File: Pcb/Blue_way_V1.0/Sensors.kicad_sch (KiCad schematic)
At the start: 0 parts

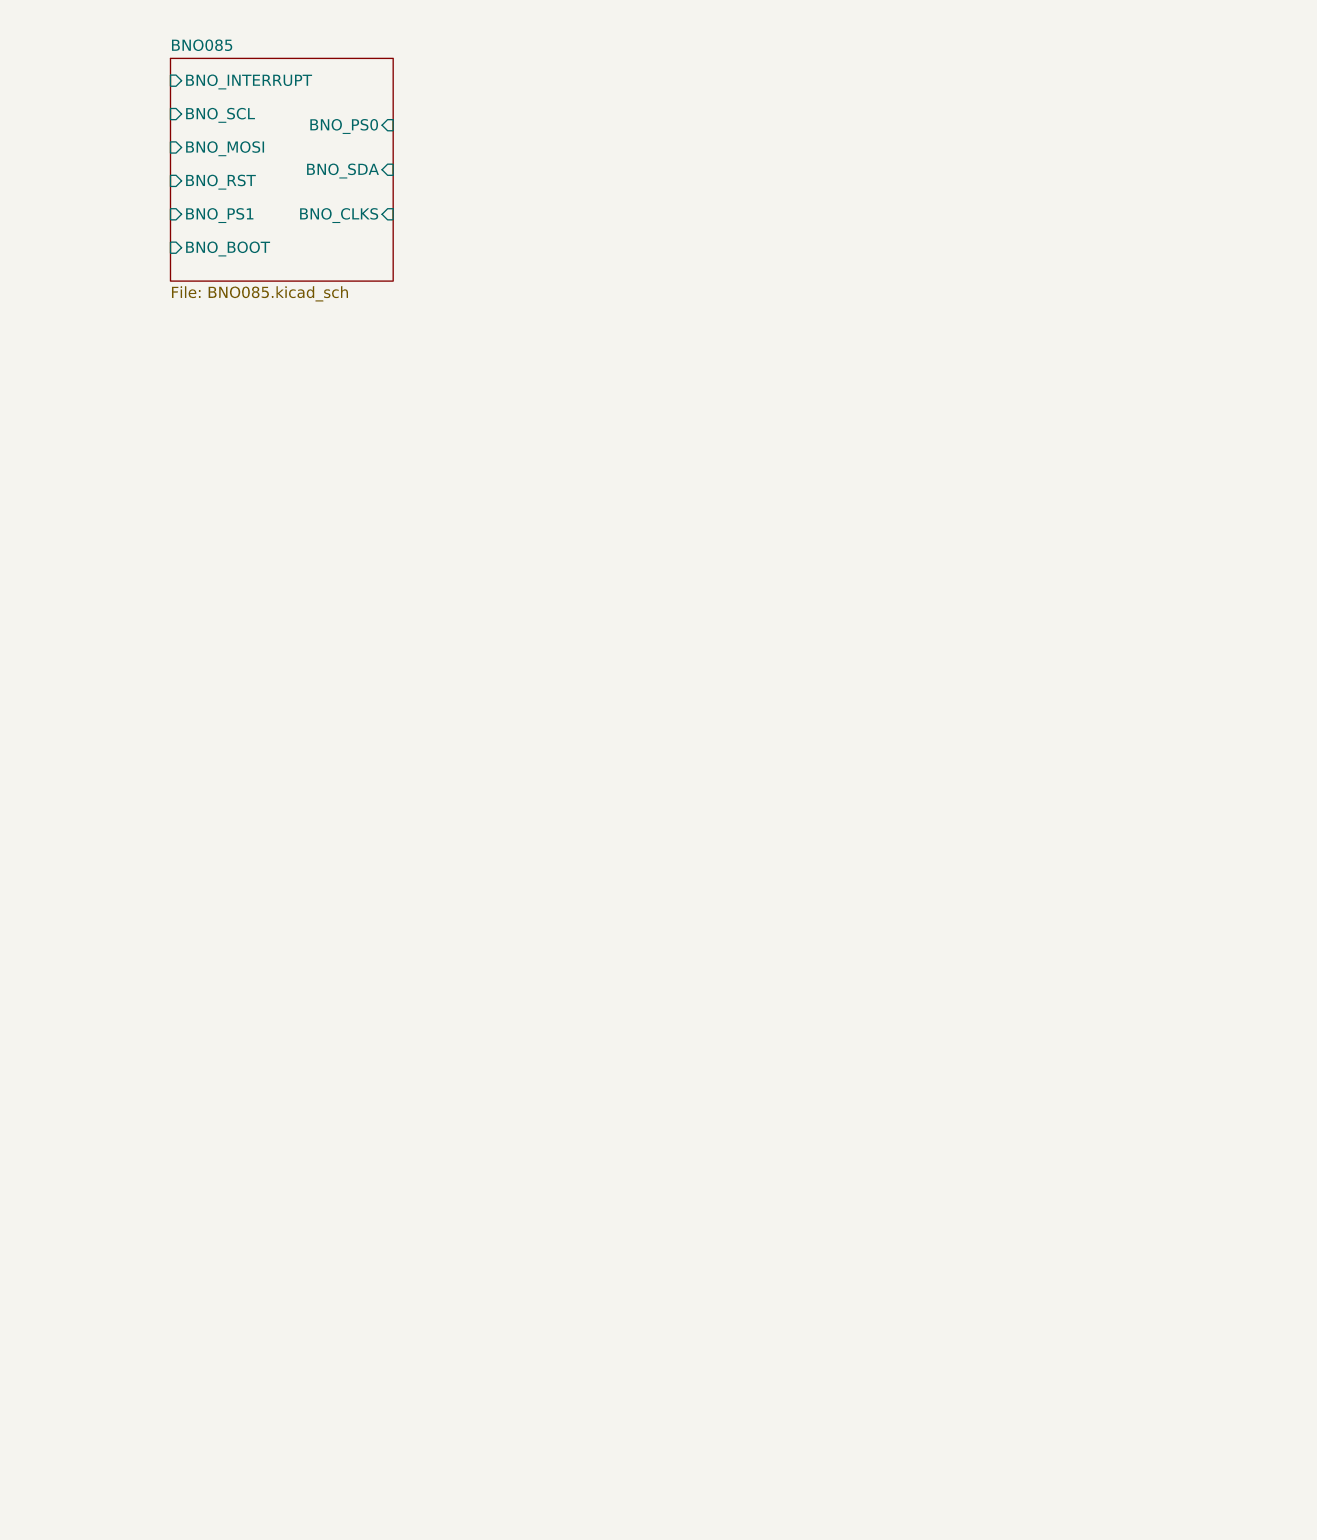
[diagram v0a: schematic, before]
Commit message: SHT and BMP Added with LoRa Comm Module
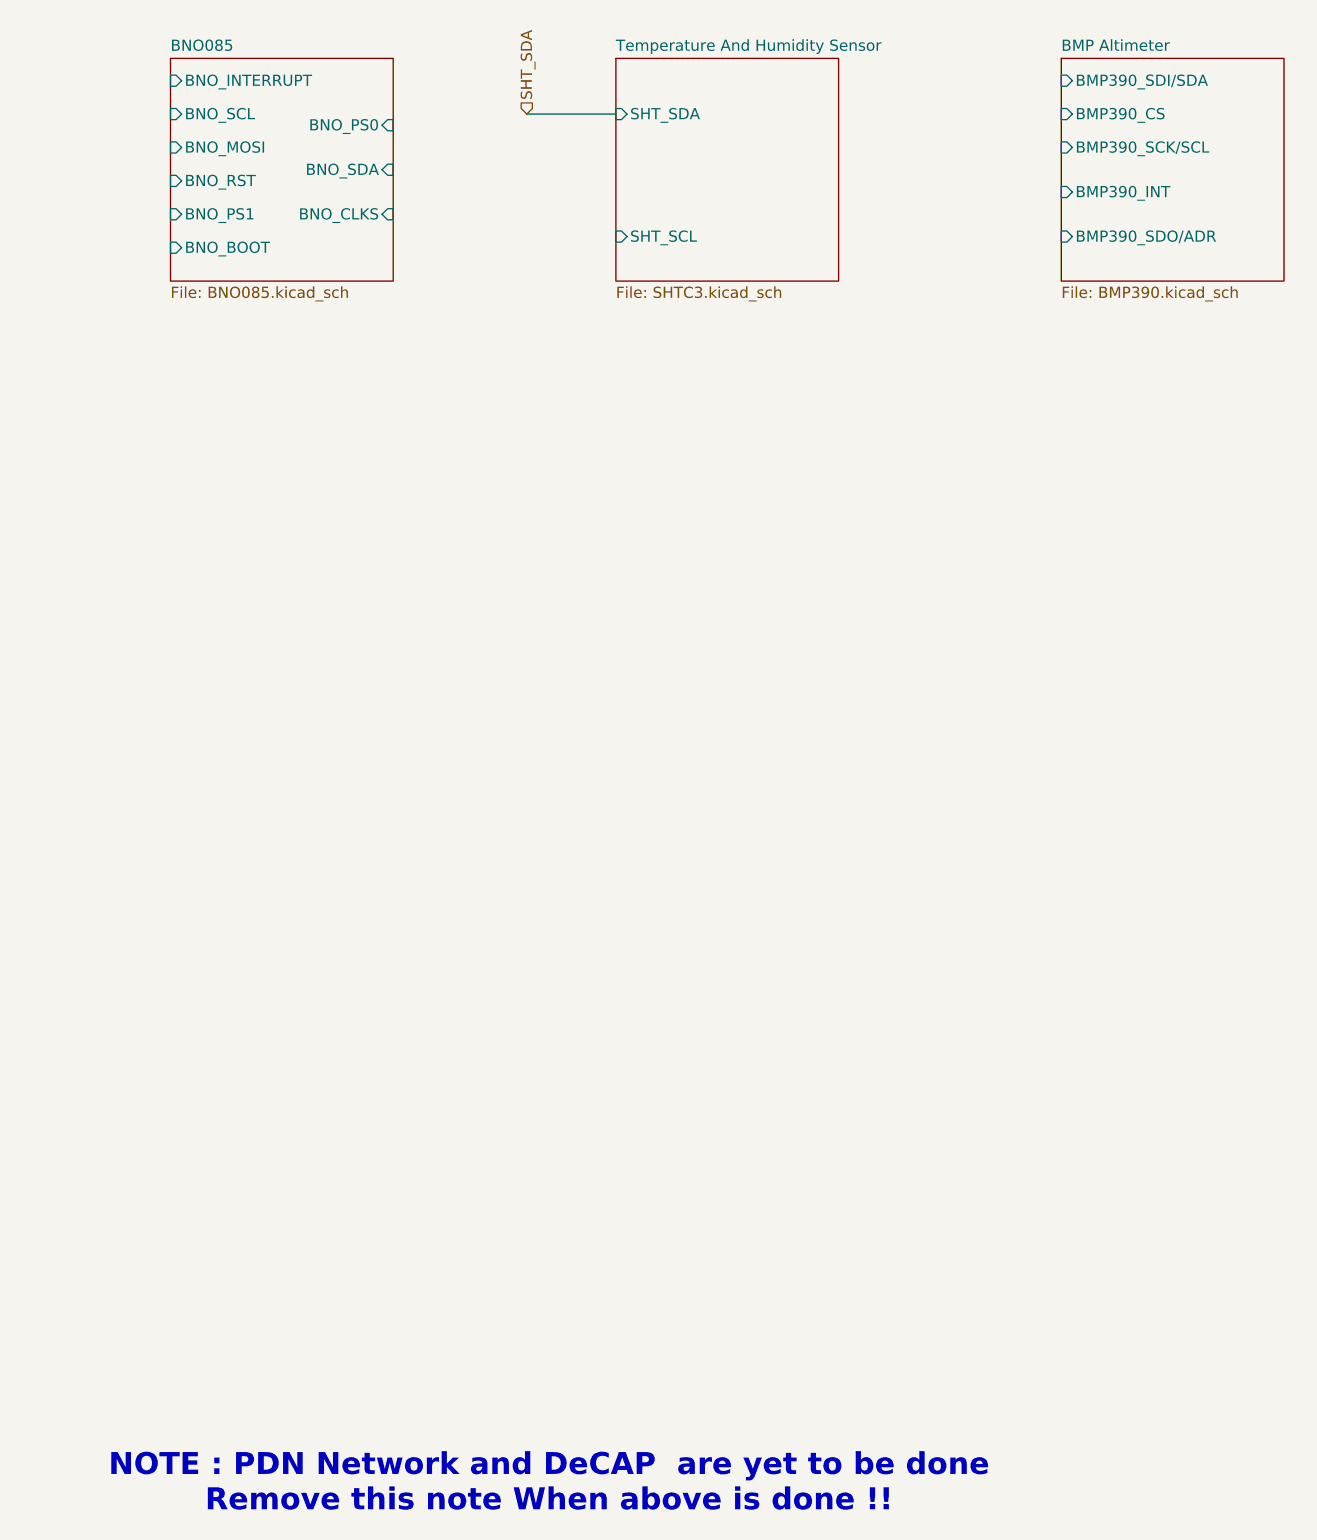
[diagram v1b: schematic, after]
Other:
- added sheet BMP Altimeter (BMP390.kicad_sch)
- added sheet Temperature And Humidity Sensor (SHTC3.kicad_sch)
- note added: "NOTE : PDN Network and DeCAP are yet to be done Remove this note When above is done !!"
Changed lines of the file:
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@@
 		(comment 1 "www.bluewayhorizon.in")
+	)
+	(text "NOTE : PDN Network and DeCAP  are yet to be done\nRemove this note When above is done !!"
+		(exclude_from_sim no)
+		(at 68.58 187.96 0)
+		(effects
+			(font
+				(size 2.5 2.5)
+				(thickness 0.5)
+				(bold yes)
+			)
+		)
+	)
+	(wire
+		(pts
+			(xy 66.04 31.75) (xy 76.2 31.75)
+		)
+		(stroke
+			(width 0)
+			(type default)
+		)
+	)
+	(hierarchical_label "SHT_SDA"
+		(shape input)
+		(at 66.04 31.75 90)
+		(effects
+			(font
+				(size 1.27 1.27)
+			)
+			(justify left)
+		)
 	)
 	(sheet
@@
 				)
 			)
+		)
+	)
+	(sheet
+		(at 127 25.4)
+		(size 25.4 25.4)
+		(exclude_from_sim no)
+		(in_bom yes)
+		(on_board yes)
+		(dnp no)
+		(fields_autoplaced yes)
+		(stroke
+			(width 0.1524)
+			(type solid)
+		)
+		(fill
+			(color 0 0 0 0.0000)
+		)
+		(property "Sheetname" "BMP Altimeter"
+			(at 127 24.6884 0)
+			(effects
+				(font
+					(size 1.27 1.27)
+				)
+				(justify left bottom)
+			)
+		)
+		(property "Sheetfile" "BMP390.kicad_sch"
+			(at 127 51.3846 0)
+			(effects
+				(font
+					(size 1.27 1.27)
+				)
+				(justify left top)
+			)
+		)
+		(pin "BMP390_SDI/SDA" input
+			(at 127 27.94 180)
+			(effects
+				(font
+					(size 1.27 1.27)
+				)
+				(justify left)
+			)
+		)
+		(pin "BMP390_CS" input
+			(at 127 31.75 180)
+			(effects
+				(font
+					(size 1.27 1.27)
+				)
+				(justify left)
+			)
+		)
+		(pin "BMP390_SCK/SCL" input
+			(at 127 35.56 180)
+			(effects
+				(font
+					(size 1.27 1.27)
+				)
+				(justify left)
+			)
+		)
+		(pin "BMP390_INT" input
+			(at 127 40.64 180)
+			(effects
+				(font
+					(size 1.27 1.27)
+				)
+				(justify left)
+			)
+		)
+		(pin "BMP390_SDO/ADR" input
+			(at 127 45.72 180)
+			(effects
+				(font
+					(size 1.27 1.27)
+				)
+				(justify left)
+			)
+		)
+		(instances
+			(project "Blue_way_V1.0"
+				(path "/2f3247fa-a7e8-4139-878f-1aed25c1e4d8/7dab7a21-a5d5-4af2-99e9-1daf90182840"
+					(page "8")
+				)
+			)
+		)
+	)
+	(sheet
+		(at 76.2 25.4)
+		(size 25.4 25.4)
+		(exclude_from_sim no)
+		(in_bom yes)
+		(on_board yes)
+		(dnp no)
+		(fields_autoplaced yes)
+		(stroke
+			(width 0.1524)
+			(type solid)
+		)
+		(fill
+			(color 0 0 0 0.0000)
+		)
+		(property "Sheetname" "Temperature And Humidity Sensor"
+			(at 76.2 24.6884 0)
+			(effects
+				(font
+					(size 1.27 1.27)
+				)
+				(justify left bottom)
+			)
+		)
+		(property "Sheetfile" "SHTC3.kicad_sch"
+			(at 76.2 51.3846 0)
+			(effects
+				(font
+					(size 1.27 1.27)
+				)
+				(justify left top)
+			)
+		)
+		(pin "SHT_SDA" input
+			(at 76.2 31.75 180)
+			(effects
+				(font
+					(size 1.27 1.27)
+				)
+				(justify left)
+			)
+		)
+		(pin "SHT_SCL" input
+			(at 76.2 45.72 180)
+			(effects
+				(font
+					(size 1.27 1.27)
+				)
+				(justify left)
+			)
+		)
+		(instances
+			(project "Blue_way_V1.0"
+				(path "/2f3247fa-a7e8-4139-878f-1aed25c1e4d8/7dab7a21-a5d5-4af2-99e9-1daf90182840"
+					(page "7")
+				)
+			)
